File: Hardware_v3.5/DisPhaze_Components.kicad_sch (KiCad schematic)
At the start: 89 parts, among them J1 SWD_Header, J2 USB_B_Micro, J3 PItch_In, J4 PD1_Amt_In, J5 PD2_Amt_In, J6 VCA_In, J7 DAC1_Out, J8 DAC2_Out, J9 Eurorack_16_pin_power, Q1 MMBT3904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

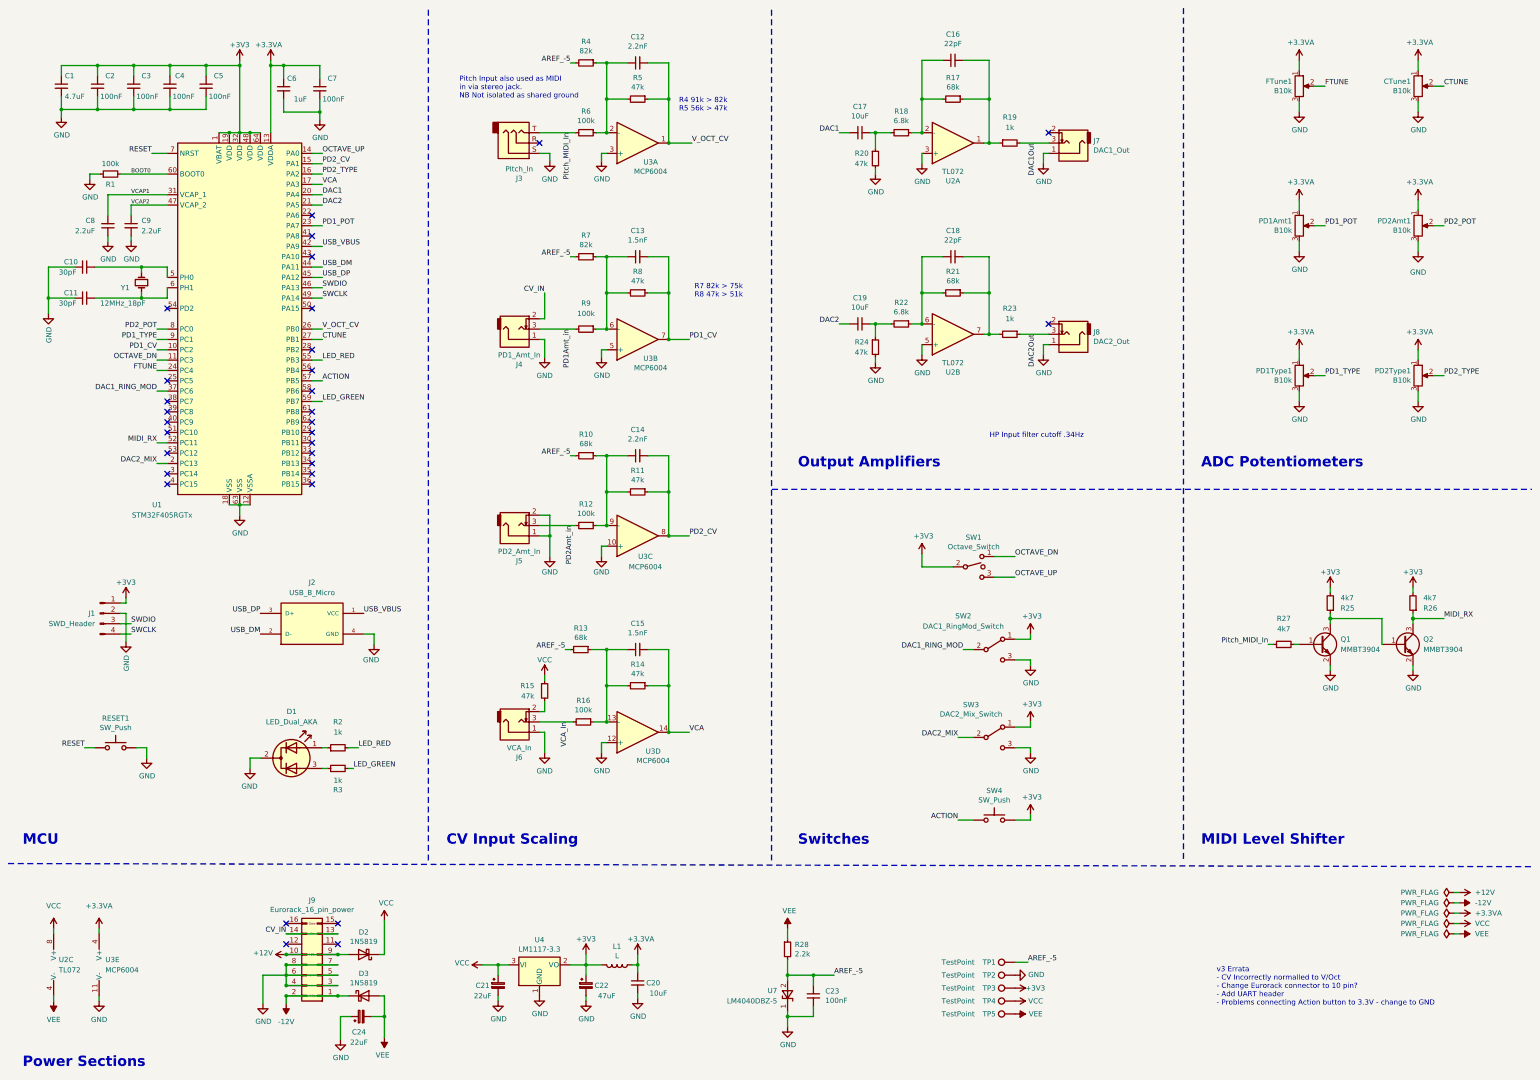
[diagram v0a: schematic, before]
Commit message: Fixed pd1 not responding in mono mode
Split original v3 schematics
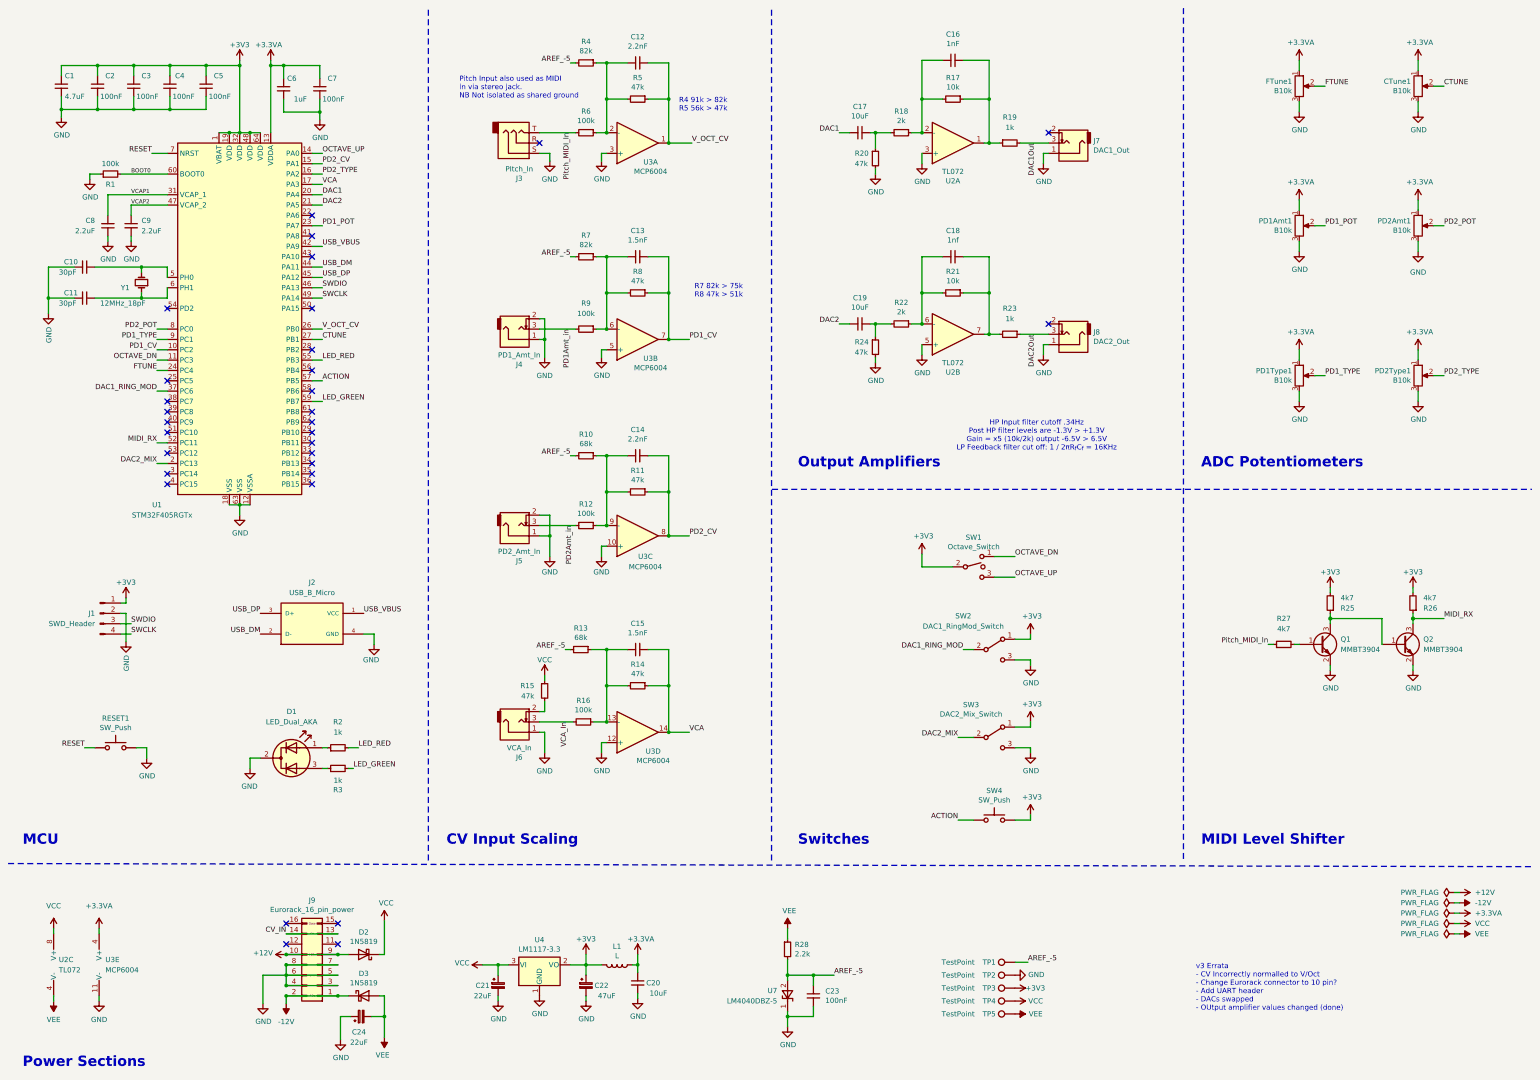
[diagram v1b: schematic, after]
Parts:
- C16: value 22pF -> 1nF
- C18: value 22pF -> 1nf
- R17, R21: value 68k -> 10k
- R18, R22: value 6.8k -> 2k
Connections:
- net CV_IN: no longer J4.2
- net GND: now also J4.2
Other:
- note added: "HP Input filter cutoff .34Hz Post HP filter levels are -1.3V > +1.3V Gain = x5 (10k/2k) output -6.5V > 6.5V LP Feedback filter cut off: 1 / 2πR_{f}C_{f} = 16KHz"
- note added: "v3 Errata - CV Incorrectly normalled to V/Oct - Change Eurorack connector to 10 pin? - Add UART header - DACs swapped - OUtput amplifier values changed (done)"
- note removed: "HP Input filter cutoff .34Hz"
- note removed: "v3 Errata - CV Incorrectly normalled to V/Oct - Change Eurorack connector to 10 pin? - Add UART header - Problems connecting Action button to 3.3V - change to GND"
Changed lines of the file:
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@@
 	)
 	(junction
+		(at 144.78 93.98)
+		(diameter 0)
+		(color 0 0 0 0)
+	)
+	(junction
 		(at 160.02 91.44)
 		(diameter 0)
@@
 	(wire
 		(pts
-			(xy 144.78 88.9) (xy 144.78 82.55)
+			(xy 144.78 88.9) (xy 144.78 93.98)
 		)
 		(stroke
@@
 		)
 	)
-	(text "v3 Errata\n- CV Incorrectly normalled to V/Oct\n- Change Eurorack connector to 10 pin?\n- Add UART header\n- Problems connecting Action button to 3.3V - change to GND"
+	(text "v3 Errata\n- CV Incorrectly normalled to V/Oct\n- Change Eurorack connector to 10 pin?\n- Add UART header\n- DACs swapped\n- OUtput amplifier values changed (done)"
 		(exclude_from_sim no)
-		(at 309.88 257.81 0)
+		(at 304.8 259.08 0)
 		(effects
 			(font
@@
 		)
 	)
-	(text "HP Input filter cutoff .34Hz"
+	(text "HP Input filter cutoff .34Hz\nPost HP filter levels are -1.3V > +1.3V\nGain = x5 (10k/2k) output -6.5V > 6.5V\nLP Feedback filter cut off: 1 / 2πR_{f}C_{f} = 16KHz"
 		(exclude_from_sim no)
 		(at 265.684 117.602 0)
@@
 		)
 	)
-	(label "CV_IN"
-		(at 144.78 82.55 180)
-		(effects
-			(font
-				(size 1.27 1.27)
-			)
-			(justify right bottom)
-		)
-	)
 	(label "PD2_TYPE"
 		(at 90.17 53.34 0)
@@
 			)
 		)
-		(property "Value" "68k"
+		(property "Value" "10k"
 			(at 245.11 79.6036 90)
 			(effects
@@
 			)
 		)
-		(property "Value" "6.8k"
+		(property "Value" "2k"
 			(at 232.41 87.2236 90)
 			(effects
@@
 			)
 		)
-		(property "Value" "68k"
+		(property "Value" "10k"
 			(at 245.11 31.9786 90)
 			(effects
@@
 			)
 		)
-		(property "Value" "6.8k"
+		(property "Value" "2k"
 			(at 232.41 40.2336 90)
 			(effects
@@
 			)
 		)
-		(property "Value" "22pF"
+		(property "Value" "1nf"
 			(at 245.11 69.5706 90)
 			(effects
@@
 			)
 		)
-		(property "Value" "22pF"
+		(property "Value" "1nF"
 			(at 245.11 21.3106 90)
 			(effects
